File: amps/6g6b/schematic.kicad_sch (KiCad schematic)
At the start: 91 parts, among them T1 125P7A, T3 125A13A

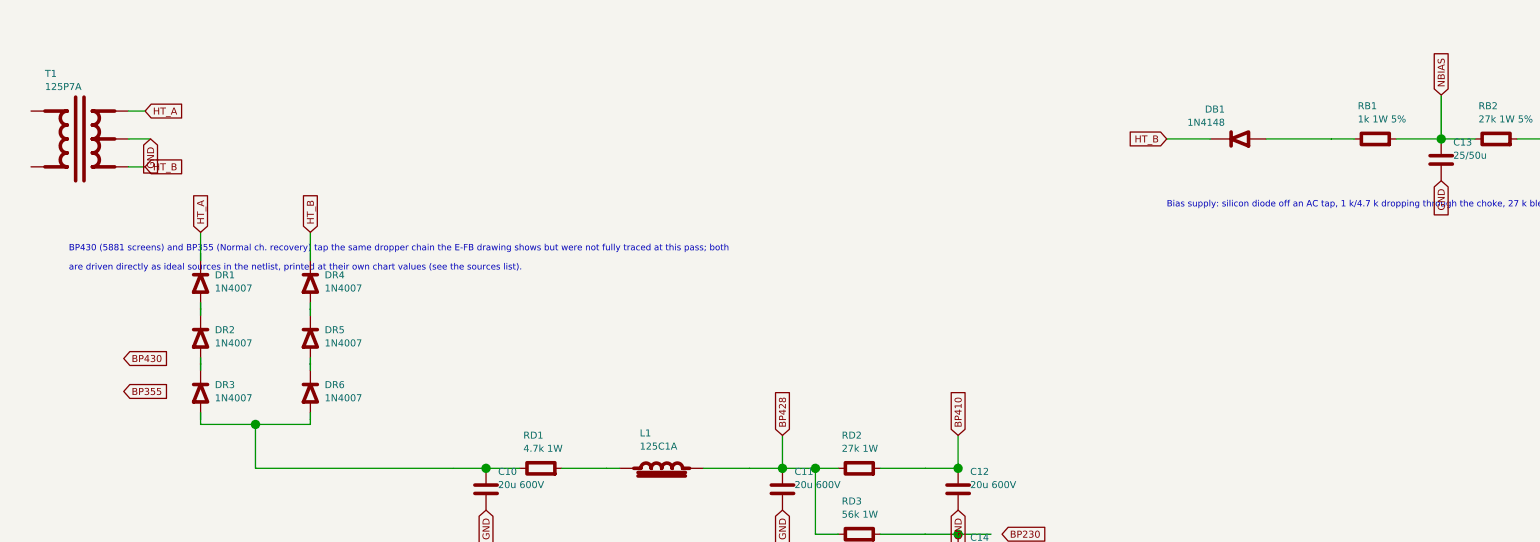
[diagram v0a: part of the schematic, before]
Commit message: Fix: 17 bias rectifiers and six HT diodes drawn backwards; the 6G6-B and 6G4 bias rows as their drawings show; AA1164 V4 units
Rectifier polarity has no gate. The netlists model every supply as an ideal
source, the sheet-vs-board check treats a two-terminal part as unordered, and
the boards' `cathode:` fields were copied from the sheets. Measured over all
68 diodes on 40 sheets: 18 negative-bias rectifiers had the cathode on the
negative node (a diode that way round would charge the node POSITIVE), and all
six 6G6-B HT diodes pointed away from B+. The printed negative bias on each of
those sheets falsifies the drawn orientation; the nine bias rectifiers already
right (AA1164, AA864, AB165, B15N, DR103, JTM100, M1959, M2204, 6G6-B) show
the idiom. Flipped: 5E4-A, 5E5-A, 5E6-A, 5F10, 5F4, 5F6, 5F6-A, 5F8-A, 5G9,
6G2, 6G3, 6G4, 6G5, AA964, AB763, AB763 Super, AB763 Twin, JTM45 (the
M1987's is with the Marshall board repair) and the 6G6-B's DR1-DR6. The
5F8-A board, which had copied its sheet, has the band moved to the tap side;
the other boards' bands are with the board-repair wave. A gate is next.

6G6-B bias. E-FB (6431x3364): the 1K 1W rises from TR1's SECOND secondary
terminal, a bias tap between the upper HT end and the grounded centre tap,
to the diode's + end. The sheet fed the diode from the HT end with the 1K
after it. T1 now carries its tap pin and the row reads tap -> 1K -> diode ->
-54 V. (The triage had read "HT end"; the native crop shows the tap.)

6G4 bias. A-FJ, read natively: tap -> rectifier -> 8 uF -> 10K -> the -55 V
node, which carries a second 8 uF and the 56K to ground as a bleeder. The
sheet fed the rectifier from an HT end, drew the 56K in series and carried
one capacitor. CBIAS2 joins the parts list, and RBIAS1's role now says
bleeder.

AA1164 V4. The K-FD sheet prints the phase inverter 7/6/8 and the tremolo
oscillator 2/1/3 (5554x4346); the sheet had them the other way round.

Gates: check_schematics 40/0 (+selftest), verify_schematic_nets 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
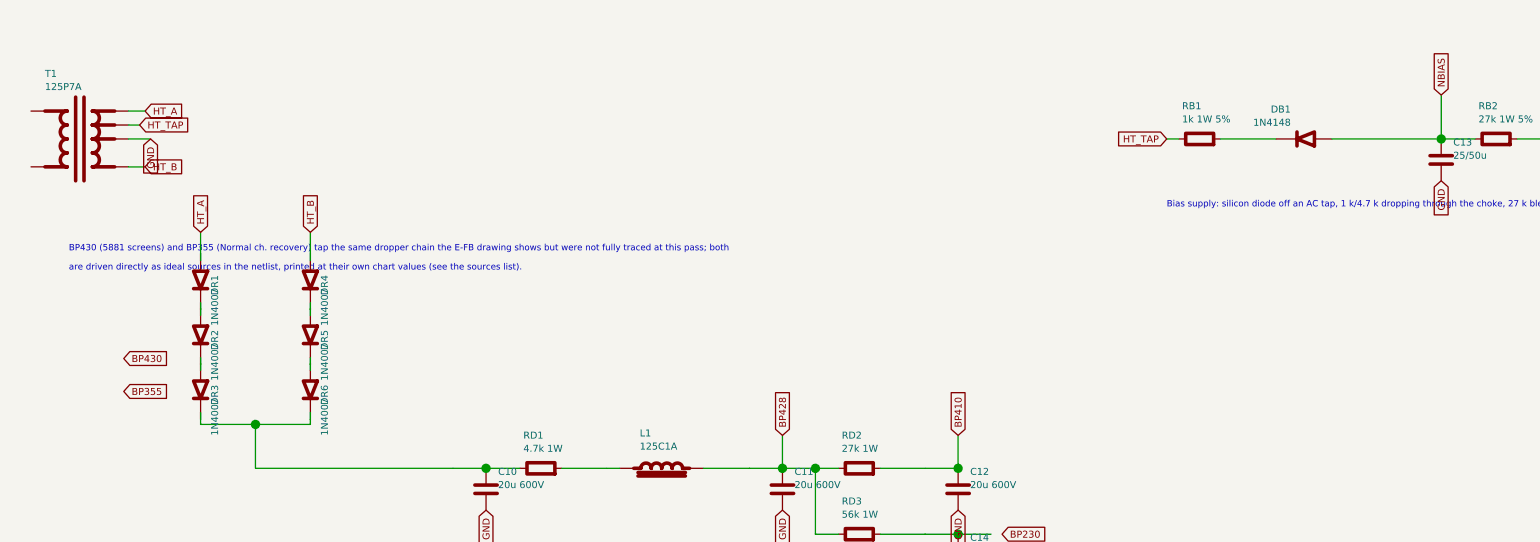
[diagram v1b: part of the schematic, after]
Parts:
- removed DR1, DR4: 1N4007, symbol cx:DIODE_SS
- added DR3, DR6: 1N4007, symbol cx:DIODE_SS
- renumbered DR3 to DR1, DR6 to DR4
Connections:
- net HT_A: now also DR1.1 (A)
- net HT_B: now also DR4.1 (A); no longer DB1.2 (K)
- net NBIAS: now also DB1.1 (A); no longer RB1.2
- net at C10.1, RD1.1: now also DR3.2 (K), DR6.2 (K); no longer DR1.1 (A), DR4.1 (A)
- net HT_TAP: now reaches RB1.1
- net HT_TAP: now also T1.6 (HT_TAP); no longer DB1.1 (A)
- net at DR2.2 (K): now also DR3.1 (A)
- net at DR5.2 (K): now also DR6.1 (A)
- new net: DB1.2 (K), RB1.2
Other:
- moved on the sheet: DR1, DR4
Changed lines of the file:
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@@
     (property "Reference" "T1" (at 15.24 288.105 0) (effects (font (size 1.27 1.27)) (justify left)))
     (property "Value" "125P7A" (at 15.24 290.505 0) (effects (font (size 1.27 1.27)) (justify left))))
+  (wire (pts (xy 30.48 297.465) (xy 32.48 297.465))
+    (stroke (width 0) (type default)))
+  (global_label "HT_TAP" (shape input) (at 32.48 297.465 0)
+    (effects (font (size 1.27 1.27)) (justify left)))
   (wire (pts (xy 30.48 300.005) (xy 34.48 300.005))
     (stroke (width 0) (type default)))
@@
   (global_label "HT_B" (shape input) (at 33.48 305.085 0)
     (effects (font (size 1.27 1.27)) (justify left)))
-  (symbol (lib_id "cx:DIODE_SS") (at 43.59 326.005 90) (unit 1)
-    (in_bom yes) (on_board yes)
-    (property "Reference" "DR1" (at 46.19 324.805 270) (effects (font (size 1.27 1.27)) (justify left)))
-    (property "Value" "1N4007" (at 46.19 327.205 270) (effects (font (size 1.27 1.27)) (justify left))))
-  (symbol (lib_id "cx:DIODE_SS") (at 43.59 336.005 90) (unit 1)
-    (in_bom yes) (on_board yes)
-    (property "Reference" "DR2" (at 46.19 334.805 270) (effects (font (size 1.27 1.27)) (justify left)))
-    (property "Value" "1N4007" (at 46.19 337.205 270) (effects (font (size 1.27 1.27)) (justify left))))
-  (symbol (lib_id "cx:DIODE_SS") (at 43.59 346.005 90) (unit 1)
-    (in_bom yes) (on_board yes)
-    (property "Reference" "DR3" (at 46.19 344.805 270) (effects (font (size 1.27 1.27)) (justify left)))
-    (property "Value" "1N4007" (at 46.19 347.205 270) (effects (font (size 1.27 1.27)) (justify left))))
+  (symbol (lib_id "cx:DIODE_SS") (at 43.59 326.005 270) (unit 1)
+    (in_bom yes) (on_board yes)
+    (property "Reference" "DR1" (at 46.19 324.805 0) (effects (font (size 1.27 1.27)) (justify left)))
+    (property "Value" "1N4007" (at 46.19 327.205 0) (effects (font (size 1.27 1.27)) (justify left))))
+  (symbol (lib_id "cx:DIODE_SS") (at 43.59 336.005 270) (unit 1)
+    (in_bom yes) (on_board yes)
+    (property "Reference" "DR2" (at 46.19 334.805 0) (effects (font (size 1.27 1.27)) (justify left)))
+    (property "Value" "1N4007" (at 46.19 337.205 0) (effects (font (size 1.27 1.27)) (justify left))))
+  (symbol (lib_id "cx:DIODE_SS") (at 43.59 346.005 270) (unit 1)
+    (in_bom yes) (on_board yes)
+    (property "Reference" "DR3" (at 46.19 344.805 0) (effects (font (size 1.27 1.27)) (justify left)))
+    (property "Value" "1N4007" (at 46.19 347.205 0) (effects (font (size 1.27 1.27)) (justify left))))
   (wire (pts (xy 43.59 320.005) (xy 43.59 320.925))
     (stroke (width 0) (type default)))
@@
   (wire (pts (xy 43.59 320.005) (xy 43.59 317.005))
     (stroke (width 0) (type default)))
-  (symbol (lib_id "cx:DIODE_SS") (at 63.59 326.005 90) (unit 1)
-    (in_bom yes) (on_board yes)
-    (property "Reference" "DR4" (at 66.19 324.805 270) (effects (font (size 1.27 1.27)) (justify left)))
-    (property "Value" "1N4007" (at 66.19 327.205 270) (effects (font (size 1.27 1.27)) (justify left))))
-  (symbol (lib_id "cx:DIODE_SS") (at 63.59 336.005 90) (unit 1)
-    (in_bom yes) (on_board yes)
-    (property "Reference" "DR5" (at 66.19 334.805 270) (effects (font (size 1.27 1.27)) (justify left)))
-    (property "Value" "1N4007" (at 66.19 337.205 270) (effects (font (size 1.27 1.27)) (justify left))))
-  (symbol (lib_id "cx:DIODE_SS") (at 63.59 346.005 90) (unit 1)
-    (in_bom yes) (on_board yes)
-    (property "Reference" "DR6" (at 66.19 344.805 270) (effects (font (size 1.27 1.27)) (justify left)))
-    (property "Value" "1N4007" (at 66.19 347.205 270) (effects (font (size 1.27 1.27)) (justify left))))
+  (symbol (lib_id "cx:DIODE_SS") (at 63.59 326.005 270) (unit 1)
+    (in_bom yes) (on_board yes)
+    (property "Reference" "DR4" (at 66.19 324.805 0) (effects (font (size 1.27 1.27)) (justify left)))
+    (property "Value" "1N4007" (at 66.19 327.205 0) (effects (font (size 1.27 1.27)) (justify left))))
+  (symbol (lib_id "cx:DIODE_SS") (at 63.59 336.005 270) (unit 1)
+    (in_bom yes) (on_board yes)
+    (property "Reference" "DR5" (at 66.19 334.805 0) (effects (font (size 1.27 1.27)) (justify left)))
+    (property "Value" "1N4007" (at 66.19 337.205 0) (effects (font (size 1.27 1.27)) (justify left))))
+  (symbol (lib_id "cx:DIODE_SS") (at 63.59 346.005 270) (unit 1)
+    (in_bom yes) (on_board yes)
+    (property "Reference" "DR6" (at 66.19 344.805 0) (effects (font (size 1.27 1.27)) (justify left)))
+    (property "Value" "1N4007" (at 66.19 347.205 0) (effects (font (size 1.27 1.27)) (justify left))))
   (wire (pts (xy 63.59 320.005) (xy 63.59 320.925))
     (stroke (width 0) (type default)))
@@
   (global_label "BP355" (shape input) (at 29.59 346.005 0)
     (effects (font (size 1.27 1.27)) (justify left)))
-  (global_label "HT_B" (shape input) (at 219.59 300.005 180)
-    (effects (font (size 1.27 1.27)) (justify right)))
-  (wire (pts (xy 219.59 300.005) (xy 227.51 300.005))
-    (stroke (width 0) (type default)))
-  (symbol (lib_id "cx:DIODE_SS") (at 232.59 300.005 180) (unit 1)
-    (in_bom yes) (on_board yes)
-    (property "Reference" "DB1" (at 230.19 294.605 0) (effects (font (size 1.27 1.27)) (justify left)))
-    (property "Value" "1N4148" (at 230.19 297.005 0) (effects (font (size 1.27 1.27)) (justify left))))
-  (wire (pts (xy 237.67 300.005) (xy 249.59 300.005))
-    (stroke (width 0) (type default)))
-  (symbol (lib_id "cx:R") (at 257.59 300.005 90) (unit 1)
-    (in_bom yes) (on_board yes)
-    (property "Reference" "RB1" (at 254.39 294.005 270) (effects (font (size 1.27 1.27)) (justify left)))
-    (property "Value" "1k 1W 5%" (at 254.39 296.405 270) (effects (font (size 1.27 1.27)) (justify left))))
-  (wire (pts (xy 249.59 300.005) (xy 253.78 300.005))
-    (stroke (width 0) (type default)))
-  (wire (pts (xy 261.4 300.005) (xy 269.59 300.005))
+  (global_label "HT_TAP" (shape input) (at 219.59 300.005 180)
+    (effects (font (size 1.27 1.27)) (justify right)))
+  (symbol (lib_id "cx:R") (at 225.59 300.005 90) (unit 1)
+    (in_bom yes) (on_board yes)
+    (property "Reference" "RB1" (at 222.39 294.005 270) (effects (font (size 1.27 1.27)) (justify left)))
+    (property "Value" "1k 1W 5%" (at 222.39 296.405 270) (effects (font (size 1.27 1.27)) (justify left))))
+  (wire (pts (xy 219.59 300.005) (xy 221.78 300.005))
+    (stroke (width 0) (type default)))
+  (wire (pts (xy 229.4 300.005) (xy 239.51 300.005))
+    (stroke (width 0) (type default)))
+  (symbol (lib_id "cx:DIODE_SS") (at 244.59 300.005 180) (unit 1)
+    (in_bom yes) (on_board yes)
+    (property "Reference" "DB1" (at 242.19 294.605 0) (effects (font (size 1.27 1.27)) (justify left)))
+    (property "Value" "1N4148" (at 242.19 297.005 0) (effects (font (size 1.27 1.27)) (justify left))))
+  (wire (pts (xy 249.67 300.005) (xy 269.59 300.005))
     (stroke (width 0) (type default)))
   (junction (at 269.59 300.005) (diameter 1.7) (color 0 0 0 0))
